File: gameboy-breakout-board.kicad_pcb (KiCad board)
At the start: 2 copper layers, 62 x 38 mm, 8 parts, among them J1 GB_GBC_1x32, J2 header

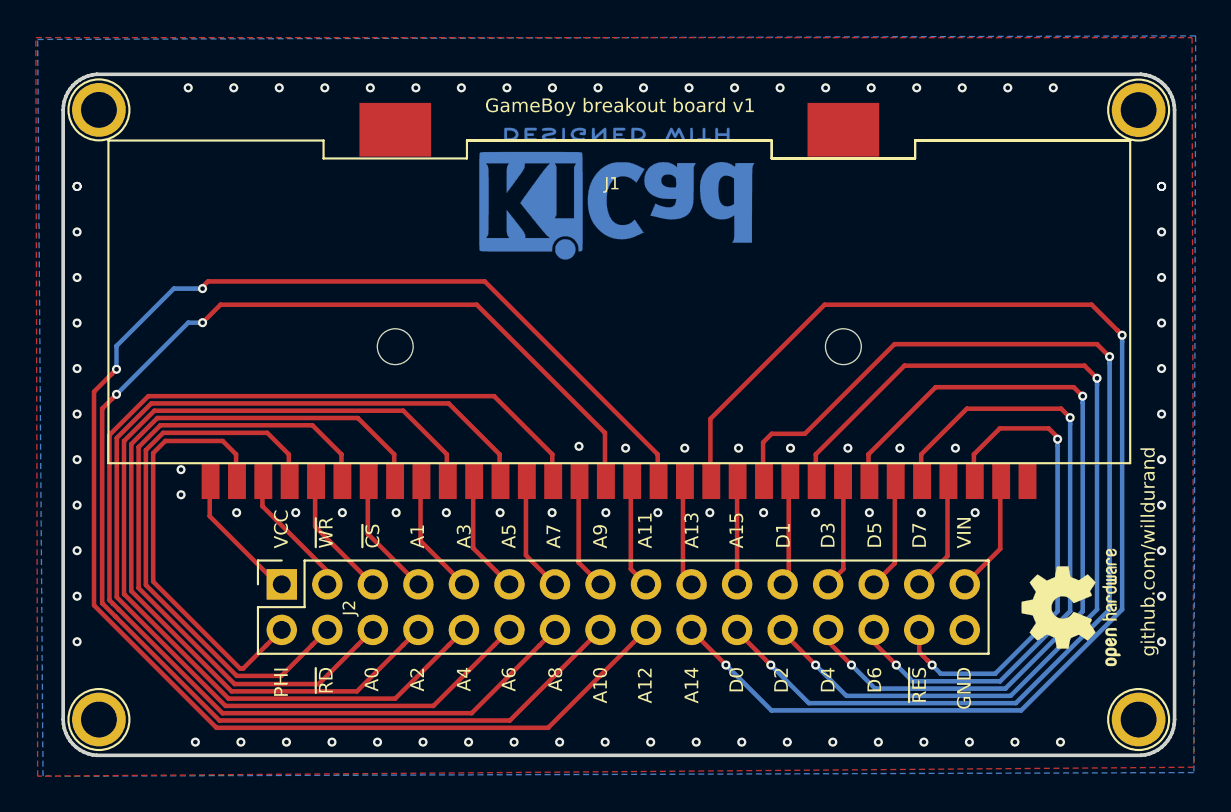
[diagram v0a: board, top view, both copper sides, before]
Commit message: Update PCB for JLCPCB
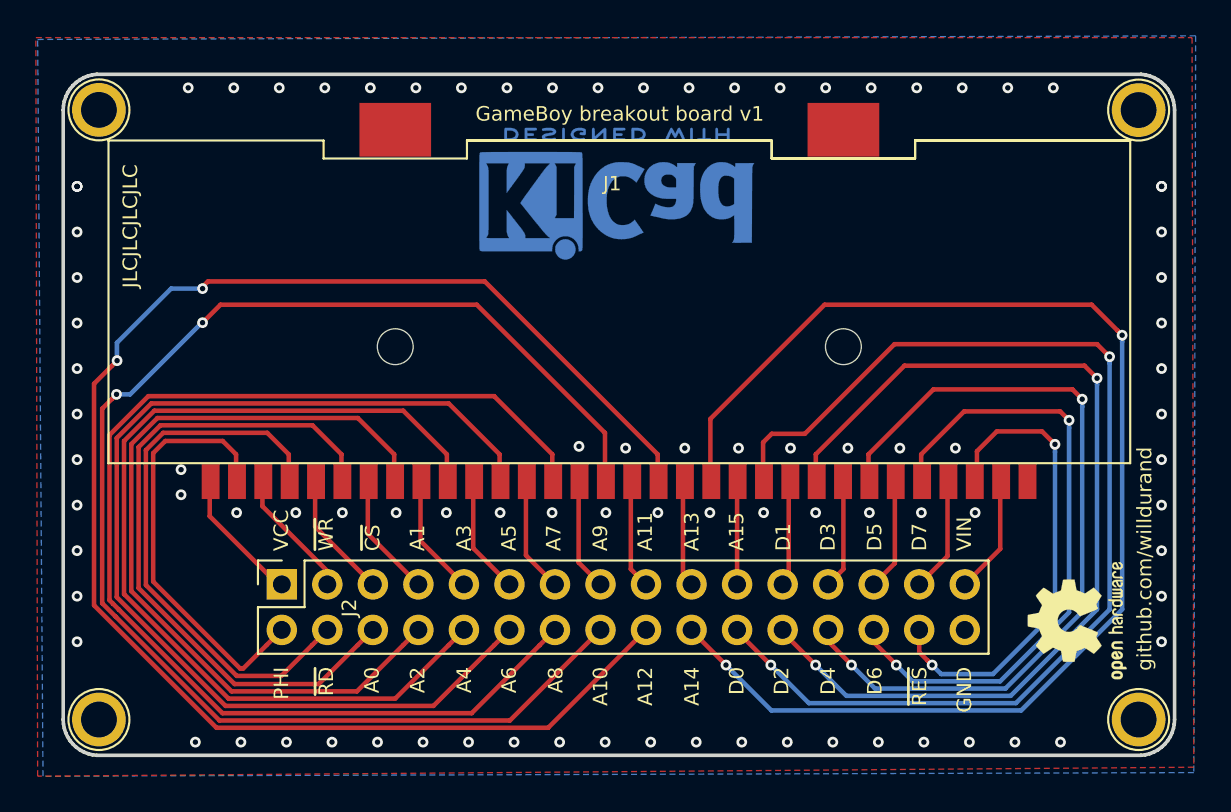
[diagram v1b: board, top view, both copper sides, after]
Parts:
- J2: value header -> Header
- moved REF** 0.81 mm to (156.6, 80.5)
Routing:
- net /~RES: track 27.5 -> 26.6 mm
- net /D0: track 62.0 -> 62.6 mm
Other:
- net class Default: clearance 0.1524 -> 0.127; trace_width 0.1524 -> 0.127; via_dia 0.508 -> 0.6; via_drill 0.254 -> 0.3
- rule pad_to_mask_clearance: 0.0508 -> 0
- rule trace_clearance: 0.1524 -> 0.127
- rule trace_min: 0.1524 -> 0.127
- rule via_min_drill: 0.254 -> 0.3
- rule via_min_size: 0.508 -> 0.6
- board text added: "JLCJLCJLCJLC"

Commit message: Fix board design
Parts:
- removed the REF** at (156.6, 80.5)
- added REF**: OSHW-Logo2_9.8x8mm_SilkScreen, Symbol:OSHW-Logo2_9.8x8mm_SilkScreen, F.Cu at (105.4, 79.8)
- moved J1 0.43 mm to (131.0, 62.8)
- moved REF** 0.42 mm to (131.2, 57.7)
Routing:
- net /A8: track 68.0 -> 67.1 mm
- net /~WR: track 7.50 -> 8.04 mm
- net /GND: vias 89 -> 70
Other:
- board text added: "GB CARD SLOT BREAKOUT BOARD"
- board text added: "williamdurand.fr"
- board text removed: "GameBoy breakout board v1"
- board text removed: "github.com/willdurand"

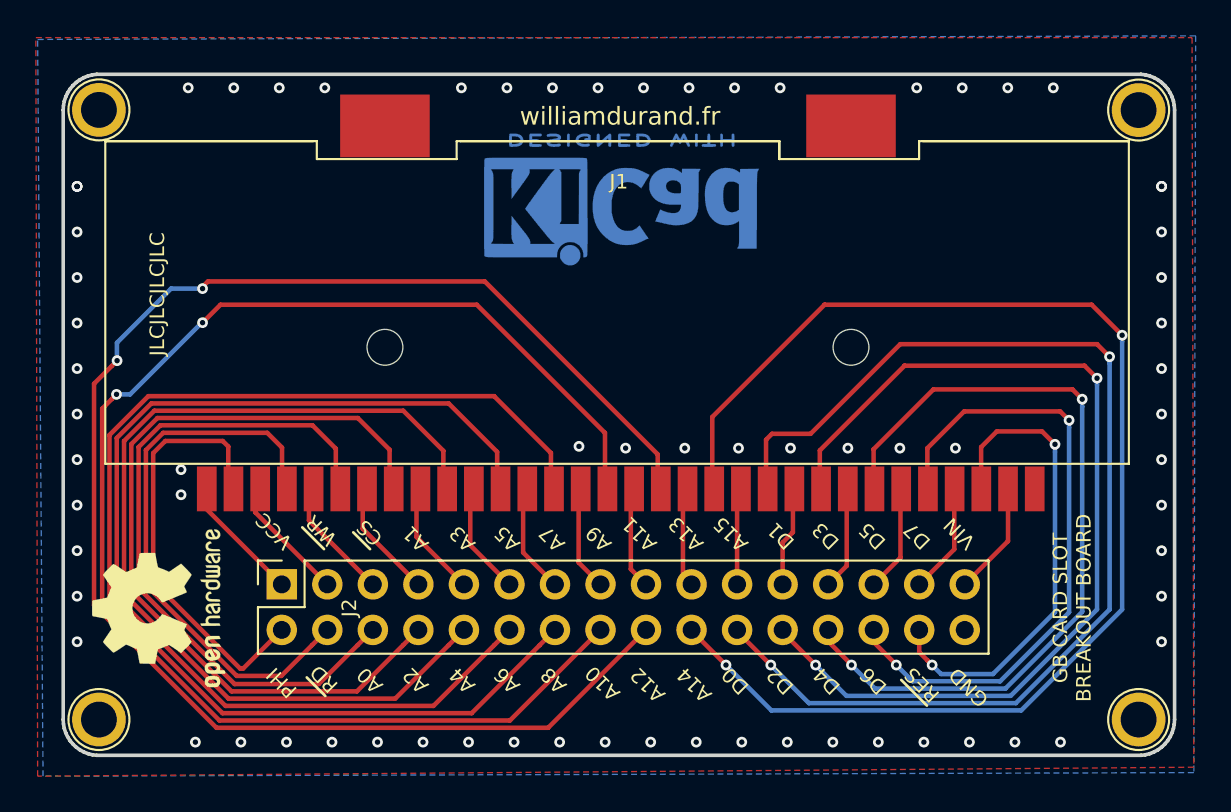
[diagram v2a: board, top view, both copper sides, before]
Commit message: Improve track clearance
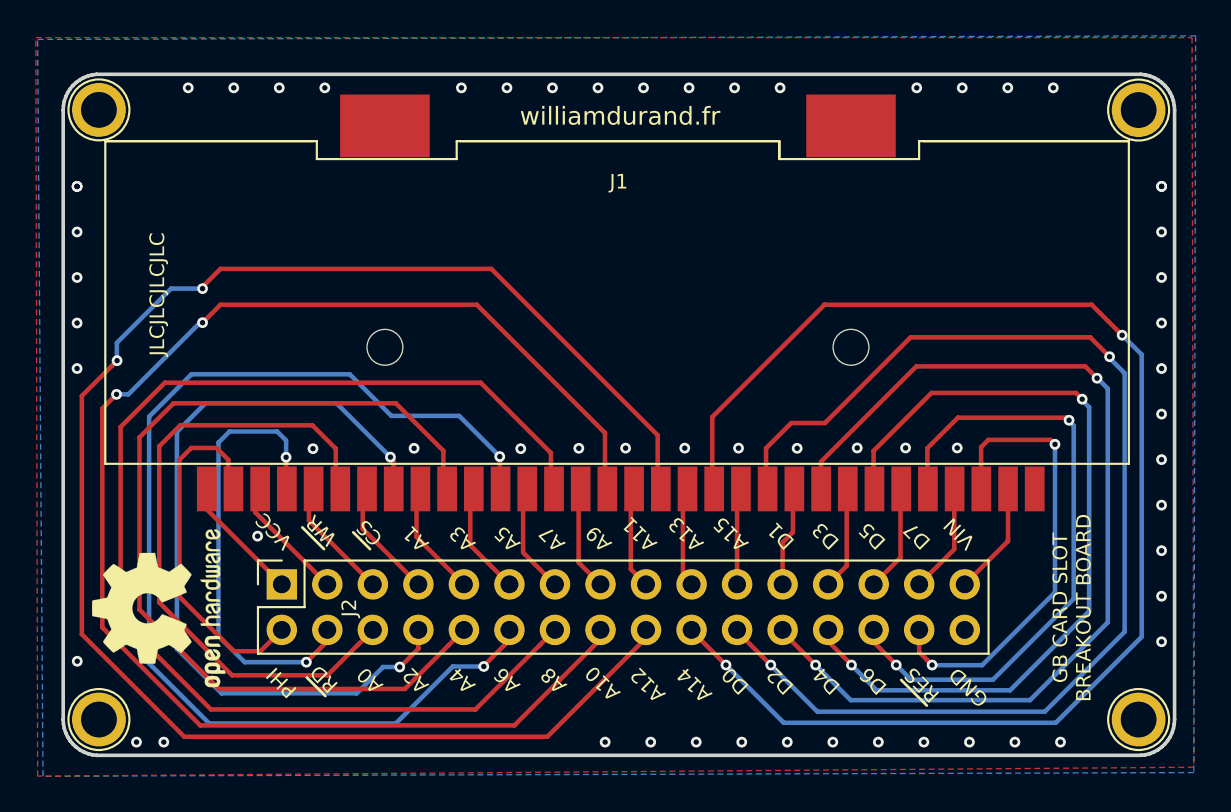
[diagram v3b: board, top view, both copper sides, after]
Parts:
- removed the REF** at (131.2, 57.7)
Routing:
- net /~RD: track 31.1 -> 25.3 mm, vias 0 -> 2
- net /PHI: track 23.9 -> 19.7 mm
- net /A12: track 88.4 -> 92.2 mm
- net /A14: track 73.4 -> 76.4 mm
- net /A6: track 59.9 -> 62.2 mm, vias 0 -> 2
- net /A0: track 38.4 -> 36.2 mm
- net /D0: track 63.1 -> 65.1 mm
- net /~RES: track 26.9 -> 25.5 mm
- net /A2: track 45.6 -> 44.2 mm, vias 0 -> 2
- net /D2: track 53.6 -> 54.9 mm
- net /A10: track 79.3 -> 80.6 mm
- net /A4: track 52.8 -> 51.6 mm
- net /GND: vias 70 -> 60
